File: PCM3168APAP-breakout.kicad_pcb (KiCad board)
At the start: 4 copper layers, 207 parts, among them IC101 PCM3168APAP, IC102 SN74LVC2G34DRLR, J101 I^{2}S, J102 I^{2}C, J103 MISC, J104 DOUT, J201 ANALOG_IN1, J202 ANALOG_IN2, J203 ANALOG_IN3, J301 OUTPUT1-4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

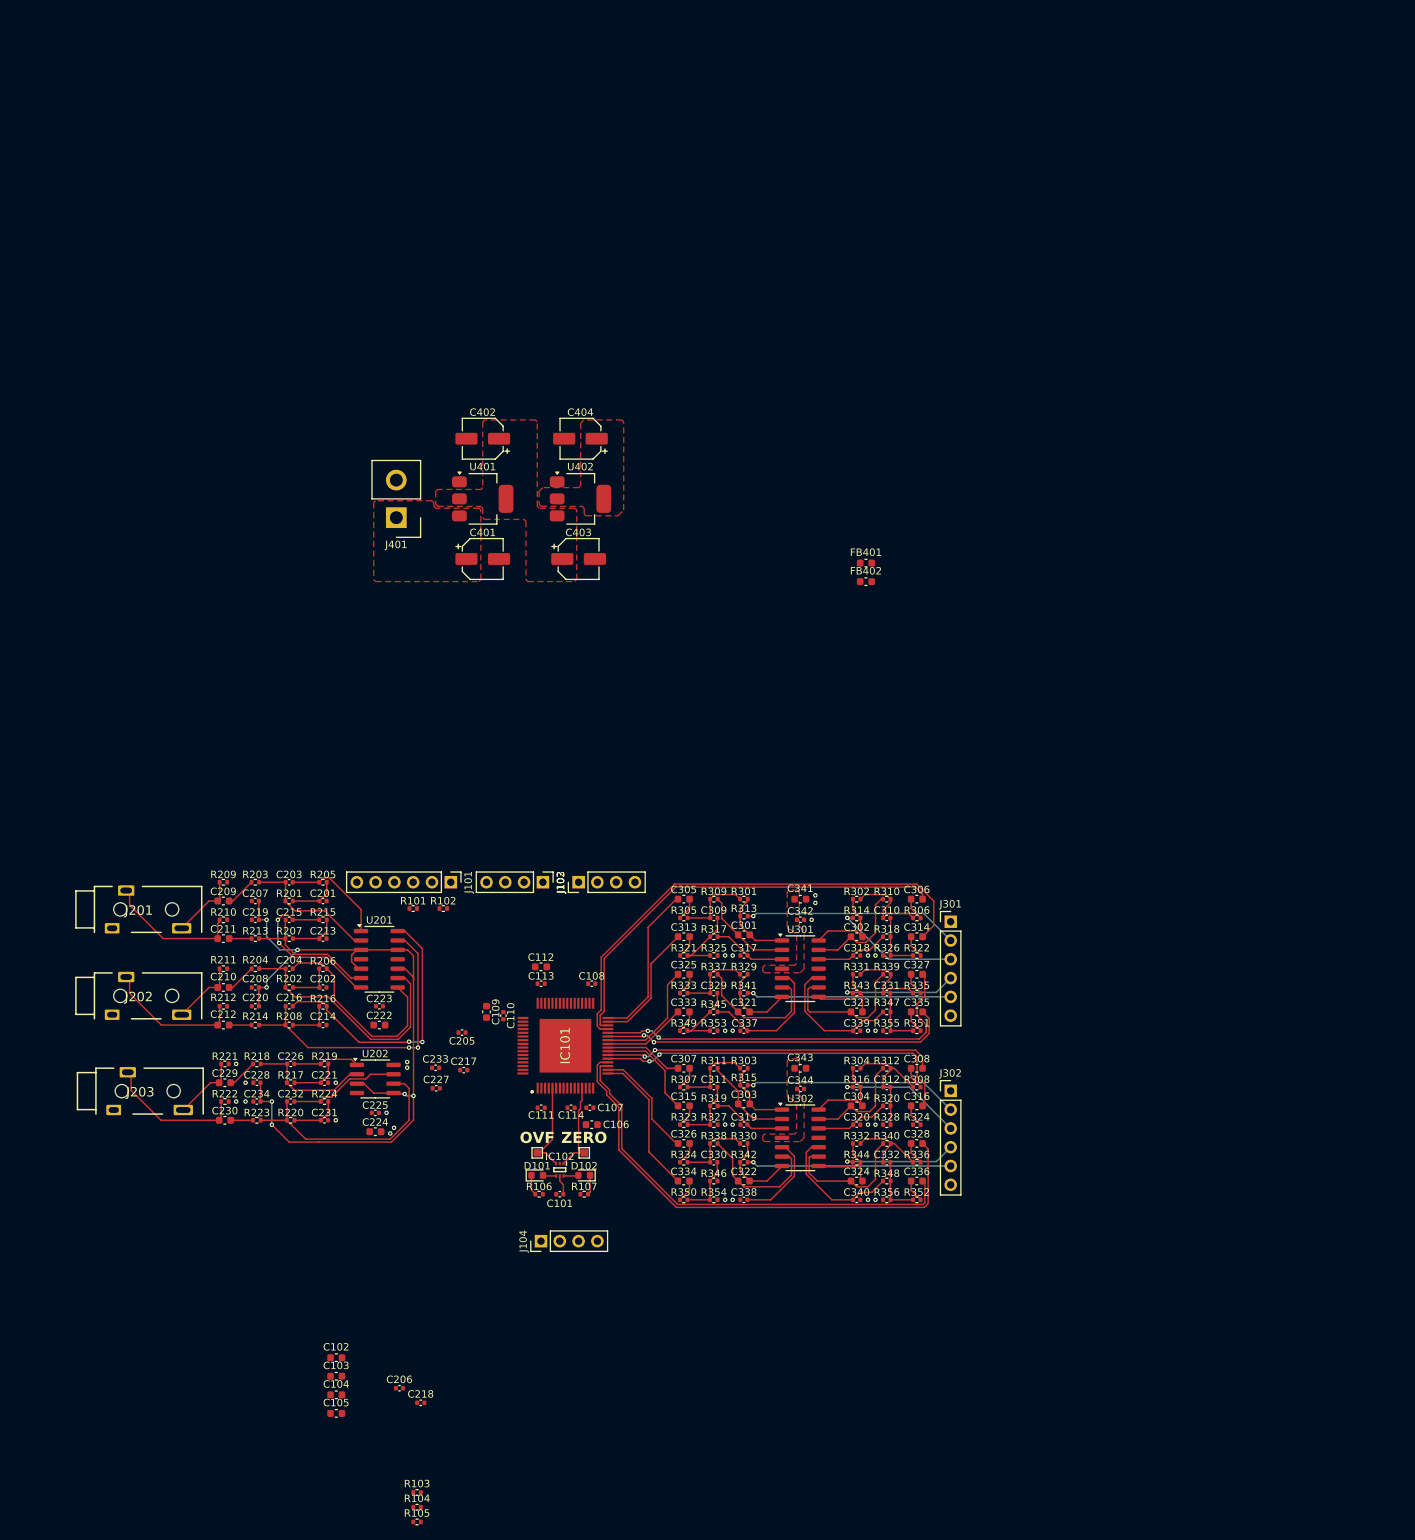
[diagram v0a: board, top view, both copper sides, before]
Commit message: Cleaned up schematic
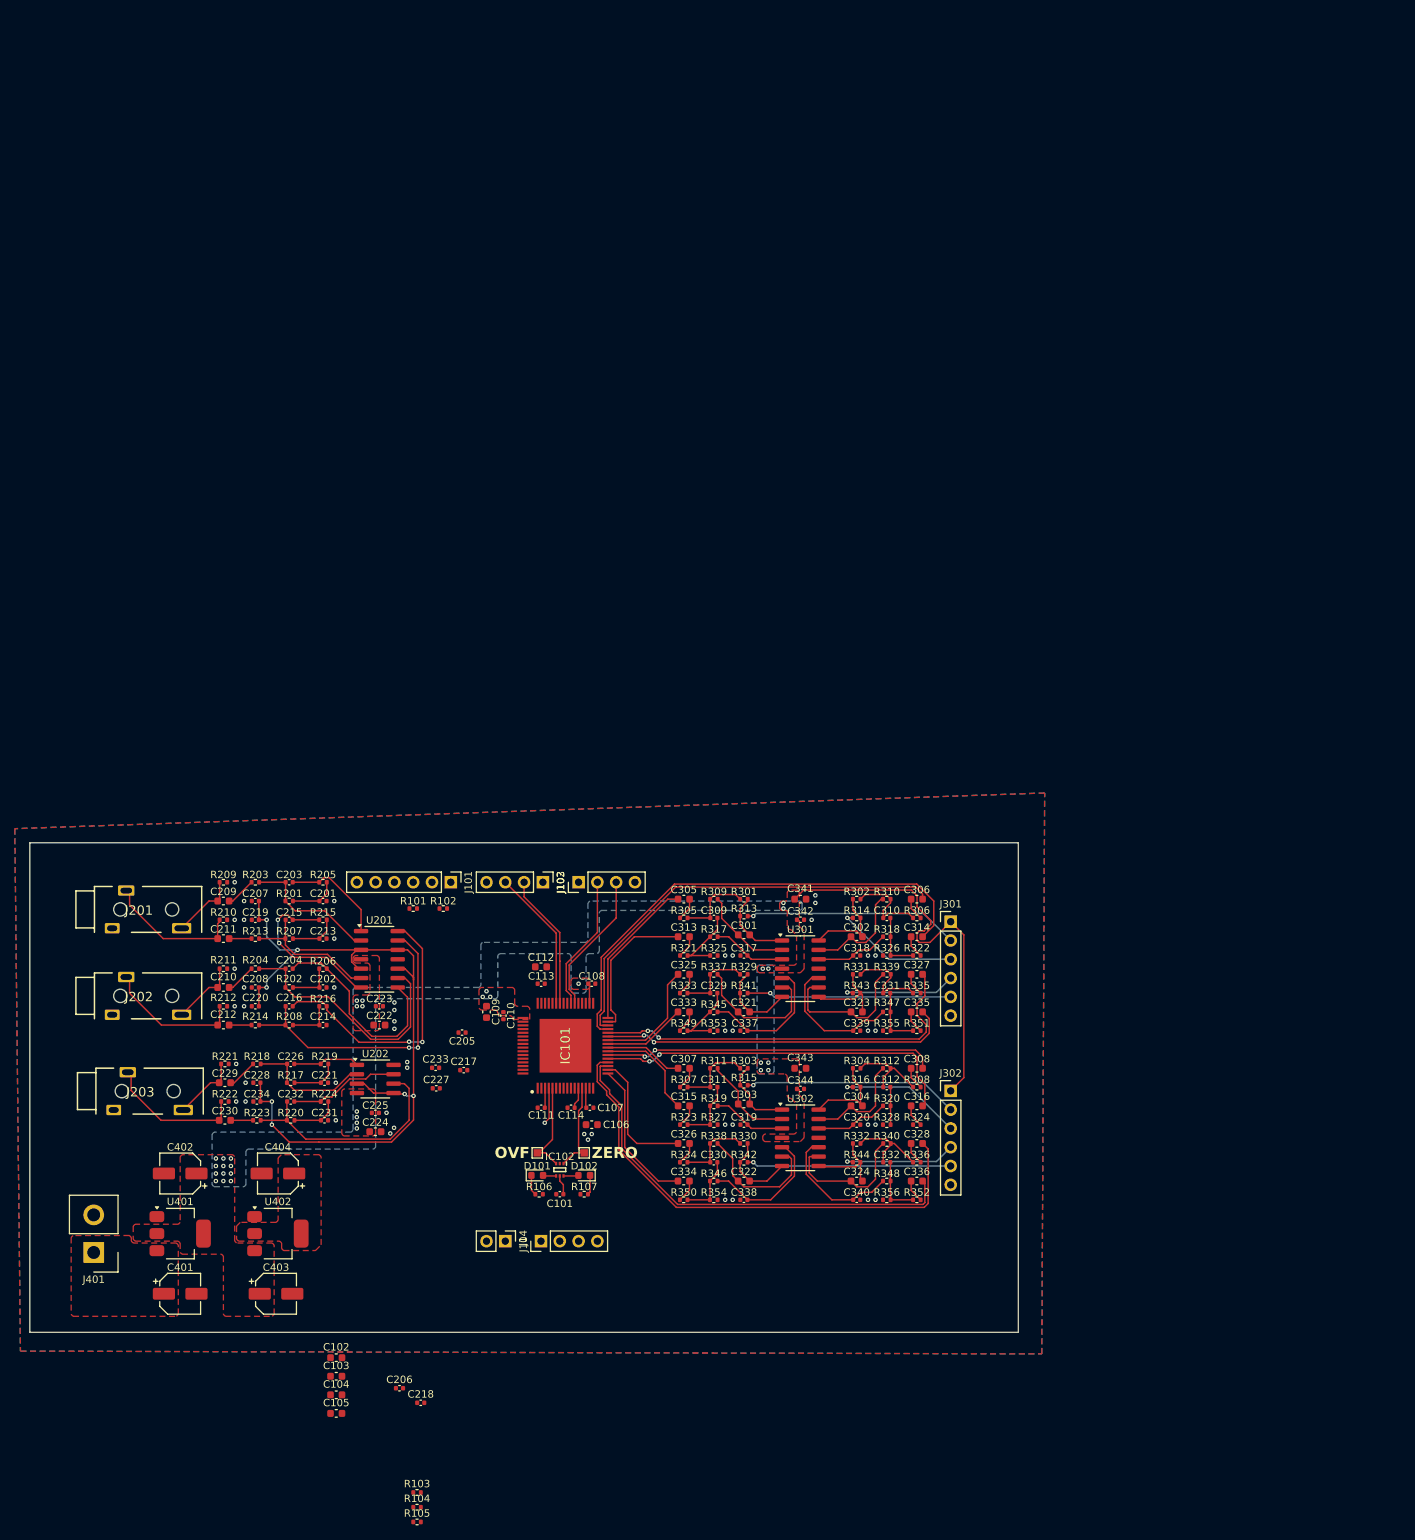
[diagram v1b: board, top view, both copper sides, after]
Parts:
- removed FB401, FB402: 220R/2A, Capacitor_SMD:C_0603_1608Metric
- added J1: ~{RESET}, Connector_PinHeader_2.54mm:PinHeader_1x02_P2.54mm_Vertical, F.Cu at (84.1, 190.8)
- J103: value MISC -> DIN
- moved C401 107.4 mm to (40.1, 197.9)
- moved C402 107.4 mm to (40.1, 181.6)
- moved C403 107.4 mm to (53.1, 197.9)
- moved J401 107.4 mm to (28.4, 192.3)
- moved U401 107.4 mm to (40.1, 189.7)
- moved U402 107.4 mm to (53.3, 189.7)
- moved C404 107.4 mm to (53.3, 181.6)
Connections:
- C101 pad 2: GNDA -> GND
- C102 pad 2: GNDA -> GND
- C103 pad 2: GNDA -> GND
- C104 pad 2: GNDA -> GND
- C105 pad 2: GNDA -> GND
- C106 pad 2: GNDA -> GND
- C107 pad 2: GNDA -> GND
- C108 pad 2: GNDA -> GND
- C109 pad 2: GNDA -> GND
- C110 pad 2: GNDA -> GND
- C111 pad 2: GNDA -> GND
- C112 pad 2: GNDA -> GND
- C113 pad 2: GNDA -> GND
- C114 pad 2: GNDA -> GND
- C201 pad 2: GNDA -> GND
- C202 pad 2: GNDA -> GND
- C205 pad 2: GNDA -> GND
- C206 pad 2: GNDA -> GND
- C207 pad 1: GNDA -> GND
- C208 pad 1: GNDA -> GND
- C213 pad 2: GNDA -> GND
- C214 pad 2: GNDA -> GND
- C217 pad 2: GNDA -> GND
- C218 pad 2: GNDA -> GND
- C219 pad 1: GNDA -> GND
- C220 pad 1: GNDA -> GND
- C221 pad 2: GNDA -> GND
- C222 pad 2: GNDA -> GND
- C223 pad 2: GNDA -> GND
- C224 pad 2: GNDA -> GND
- C225 pad 2: GNDA -> GND
- C227 pad 2: GNDA -> GND
- C228 pad 1: GNDA -> GND
- C231 pad 2: GNDA -> GND
- C233 pad 2: GNDA -> GND
- C234 pad 1: GNDA -> GND
- C317 pad 2: GNDA -> GND
- C318 pad 2: GNDA -> GND
- C319 pad 2: GNDA -> GND
- C320 pad 2: GNDA -> GND
- C337 pad 2: GNDA -> GND
- C338 pad 2: GNDA -> GND
- C339 pad 2: GNDA -> GND
- C340 pad 2: GNDA -> GND
- C341 pad 2: GNDA -> GND
- C342 pad 2: GNDA -> GND
- C343 pad 2: GNDA -> GND
- C344 pad 2: GNDA -> GND
- IC101 pad 11: GNDA -> GND
- IC101 pad 16: GNDA -> GND
- IC101 pad 2: GNDA -> GND
- IC101 pad 33: GNDA -> GND
- IC101 pad 47: GNDA -> GND
- IC101 pad 48: GNDA -> GND
- IC101 pad 50: GNDA -> GND
- IC101 pad 65: GNDA -> GND
- IC102 pad 2: GNDA -> GND
- J103 pad 1: /~{RST} -> /DIN3
- J103 pad 2: /DIN3 -> /DIN2
- J103 pad 3: /DIN2 -> /SDIN
- J201 pad S: GNDA -> GND
- J202 pad S: GNDA -> GND
- J203 pad S: GNDA -> GND
- J301 pad 6: GNDA -> GND
- J302 pad 6: GNDA -> GND
- R106 pad 2: GNDA -> GND
- R107 pad 2: GNDA -> GND
- R209 pad 2: GNDA -> GND
- R210 pad 2: GNDA -> GND
- R211 pad 2: GNDA -> GND
- R212 pad 2: GNDA -> GND
- R221 pad 2: GNDA -> GND
- R222 pad 2: GNDA -> GND
- R325 pad 1: GNDA -> GND
- R326 pad 1: GNDA -> GND
- R327 pad 1: GNDA -> GND
- R328 pad 1: GNDA -> GND
- R353 pad 1: GNDA -> GND
- R354 pad 1: GNDA -> GND
- R355 pad 1: GNDA -> GND
- R356 pad 1: GNDA -> GND
- U201 pad 11: GNDA -> GND
- U202 pad 8: GNDA -> GND
- U301 pad 11: GNDA -> GND
- U302 pad 11: GNDA -> GND
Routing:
- net +5V: track 0.00 -> 63.5 mm, vias 0 -> 35
- net /DIN2: track 0.00 -> 19.3 mm
- net /SDA: track 0.00 -> 19.2 mm
- net /DIN3: track 0.00 -> 18.4 mm
- net /SCL: track 0.00 -> 18.4 mm
- net Net-(U302B-+): track 12.5 -> 17.6 mm
- net /~{RST}: track 0.00 -> 4.93 mm, vias 0 -> 1
- net /Analog Outputs/VOUT1+: track 17.0 -> 20.0 mm
- net +3.3V: track 2.66 -> 5.52 mm
- net /Analog Outputs/VOUT8-: track 15.3 -> 17.7 mm
- net /Analog Outputs/VOUT1-: track 21.6 -> 20.8 mm
- net GNDA: vias 30 -> 0
- net GND: vias 0 -> 45
- added copper zone on B.Cu, net +5V
- added copper zone on B.Cu, net GND
- added copper zone on F.Cu, net GND
- added copper zone on In1.Cu, net GND
- added copper zone on In2.Cu, net GND
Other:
- board outline added: 133.6 x 66.2 mm

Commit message: finished routin, updated schematic, added PDF
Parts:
- moved R105 197.8 mm to (140.7, 43.2), turned to -90 degrees
- moved R103 195.4 mm to (144.5, 43.2), turned to -90 degrees
- moved R104 195.3 mm to (138.9, 43.2), turned to -90 degrees
- moved C105 170.7 mm to (134.1, 59.7), turned to 180 degrees
- moved C104 170.3 mm to (134.1, 57.7), turned to 180 degrees
- moved C103 168.2 mm to (150.6, 66.5), turned to -90 degrees
- moved C206 165.5 mm to (129.0, 56.1), turned to 180 degrees
- moved C218 164.9 mm to (129.0, 57.7), turned to 180 degrees
- moved C102 160.1 mm to (138.9, 66.5), turned to -90 degrees
- moved C403 147.1 mm to (148.5, 85.9), turned to 90 degrees
- moved C401 146.8 mm to (148.5, 98.8), turned to 90 degrees
- moved J401 140.7 mm to (142.9, 110.5), turned to -90 degrees
- moved U402 135.7 mm to (140.3, 85.6), turned to 90 degrees
- moved U401 135.3 mm to (140.3, 98.8), turned to 90 degrees
- moved J201 133.6 mm to (106.0, 38.0)
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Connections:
- C204 pad 1: Net-(U201C--) -> Net-(U201D--)
- C216 pad 1: Net-(U201D--) -> Net-(U201C--)
- C226 pad 1: Net-(U202A--) -> Net-(U202B--)
- C232 pad 1: Net-(U202B--) -> Net-(U202A--)
- R202 pad 1: Net-(U201C--) -> Net-(U201D--)
- R204 pad 2: Net-(U201C--) -> Net-(U201D--)
- R208 pad 1: Net-(U201D--) -> Net-(U201C--)
- R214 pad 2: Net-(U201D--) -> Net-(U201C--)
- R217 pad 1: Net-(U202A--) -> Net-(U202B--)
- R218 pad 2: Net-(U202A--) -> Net-(U202B--)
- R220 pad 1: Net-(U202B--) -> Net-(U202A--)
- R223 pad 2: Net-(U202B--) -> Net-(U202A--)
- U201 pad 14: Net-(C216-Pad2) -> Net-(C204-Pad2)
- U201 pad 8: Net-(C204-Pad2) -> Net-(C216-Pad2)
- U202 pad 1: Net-(C226-Pad2) -> Net-(C232-Pad2)
- U202 pad 7: Net-(C232-Pad2) -> Net-(C226-Pad2)
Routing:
- net +5V: track 63.5 -> 344.2 mm, vias 35 -> 13
- net +3.3V: track 5.52 -> 99.4 mm, vias 0 -> 5
- net /SDIN: track 0.00 -> 55.5 mm
- net /BCK_ADC: track 0.00 -> 54.1 mm, vias 0 -> 2
- net /LRCK_ADC: track 0.00 -> 53.9 mm, vias 0 -> 2
- net /Analog Inputs/VIN6+: track 6.53 -> 48.9 mm
- net /~{RST}: track 4.93 -> 46.2 mm, vias 1 -> 2
- net /Analog Inputs/VIN5+: track 6.53 -> 46.3 mm
- net /BCK_DAC: track 0.00 -> 39.6 mm, vias 0 -> 2
- net /Analog Inputs/VCOMAD: track 103.4 -> 141.9 mm, vias 7 -> 6
- net /MCLK: track 0.00 -> 38.4 mm, vias 0 -> 1
- net GND: track 0.00 -> 36.4 mm, vias 45 -> 106
- net /LRCK_DAC: track 0.00 -> 35.7 mm, vias 0 -> 2
- net /DOUT3: track 0.00 -> 34.5 mm, vias 0 -> 1
- net /Analog Inputs/VIN4+: track 6.13 -> 38.8 mm, vias 0 -> 2
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- removed copper zone on F.Cu, net +3.3V
- removed copper zone on B.Cu, net +5V
- removed copper zone on F.Cu, net +5V
- removed copper zone on F.Cu, net /Power/V_EXT
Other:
- board size 133.6 x 66.2 mm -> 100 x 85.5 mm
- board text added: "3.3V"
- board text added: "5V"
- board text added: "6.2 TO 18V"
- board text added: "AO1"
- board text added: "AO2"
- board text added: "AO3"
- board text added: "AO4"
- board text added: "AO5"
- board text added: "AO6"
- board text added: "AO7"
- board text added: "AO8"
- board text added: "BCKD"
- board text added: "DIN1"
- board text added: "DIN2"
- board text added: "DOUT1"
- board text added: "DOUT2"
- board text added: "DOUT3"
- board text added: "GND"
- board text added: "LRCD"
- board text added: "MCLK"
- board text added: "RST"
- board text added: "SCL"
- board text added: "SDA"
- board text added: "SDIN"
- board text added: "VIN"
